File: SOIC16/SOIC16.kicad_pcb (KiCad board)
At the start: 2 copper layers, 20.3 x 12.7 mm, 7 parts, among them J1 Conn_02x08_Counter_Clockwise, J2 Conn_01x08, J3 Conn_01x08

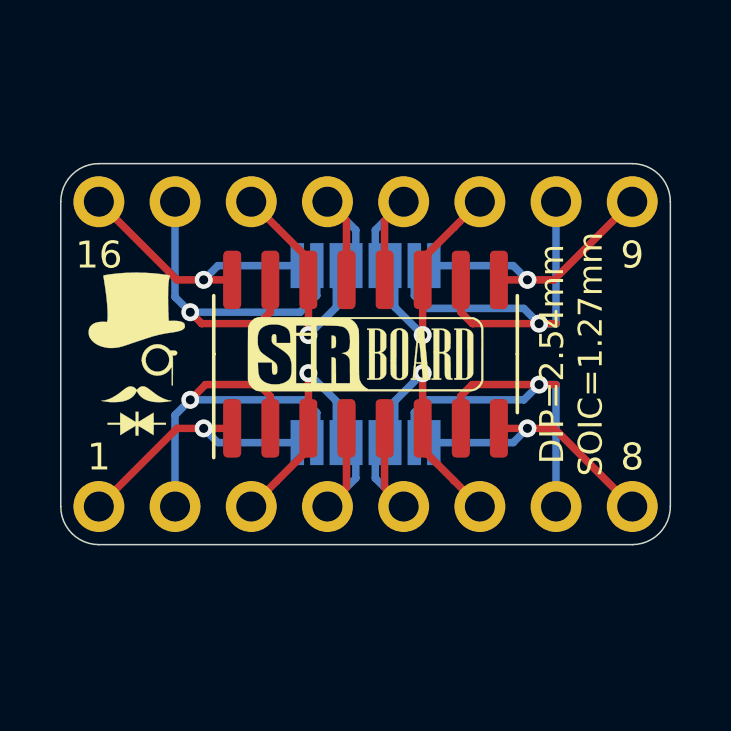
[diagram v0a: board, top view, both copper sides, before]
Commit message: convert SOIC16 to kicad 7
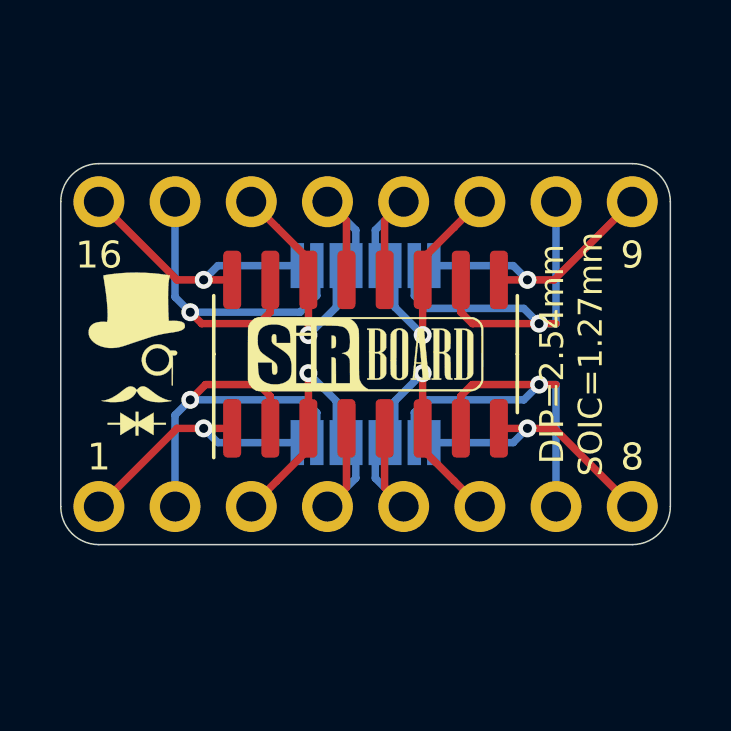
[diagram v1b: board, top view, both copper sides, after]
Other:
- net class Default removed

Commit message: add SOIC-Wide-16
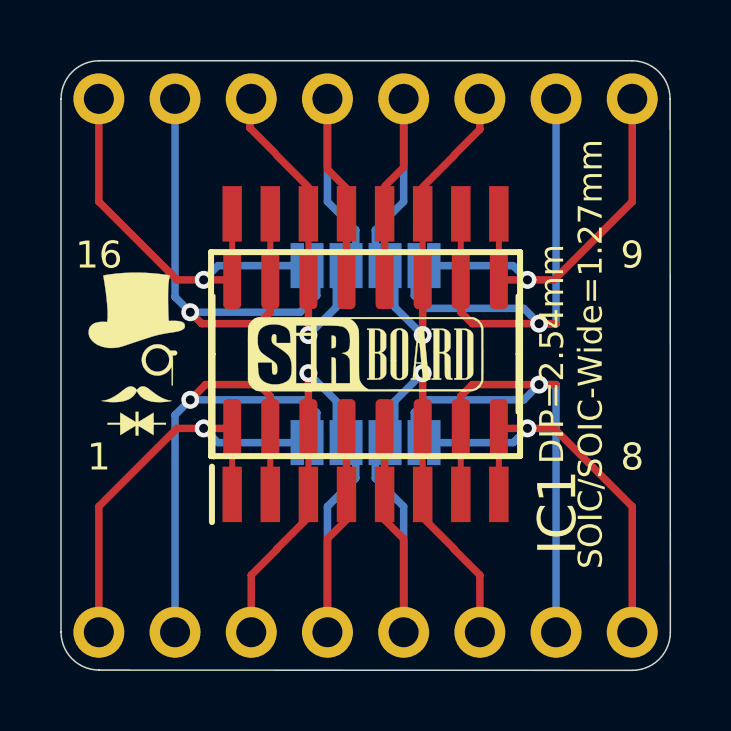
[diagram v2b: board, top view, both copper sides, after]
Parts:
- added IC1: SI8622ED-B-ISR 5kV, Kernelport:SOIC127P1030X265-16N, F.Cu at (66.4, 36.4)
- moved J3 4.19 mm to (57.5, 45.7)
- moved J2 3.43 mm to (57.5, 27.9)
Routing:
- net Net-(J1-Pad5): track 5.39 -> 12.7 mm
- net Net-(J1-Pad4): track 5.39 -> 12.7 mm
- net Net-(J1-Pad13): track 5.39 -> 11.2 mm
- net Net-(J1-Pad12): track 5.39 -> 11.1 mm
- net Net-(J1-Pad8): track 8.84 -> 13.0 mm
- net Net-(J1-Pad7): track 14.6 -> 18.8 mm
- net Net-(J1-Pad2): track 13.3 -> 17.5 mm
- net Net-(J1-Pad1): track 8.84 -> 13.0 mm
- net Net-(J1-Pad9): track 8.84 -> 12.3 mm
- net Net-(J1-Pad16): track 8.84 -> 12.3 mm
- net Net-(J1-Pad15): track 13.4 -> 16.8 mm
- net Net-(J1-Pad10): track 14.6 -> 18.0 mm
- net Net-(J1-Pad3): track 7.93 -> 9.84 mm
- net Net-(J1-Pad6): track 7.93 -> 9.84 mm
- net Net-(J1-Pad11): track 7.93 -> 8.95 mm
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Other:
- board size 20.3 x 12.7 mm -> 20.3 x 20.3 mm
- board text added: "DIP=2.54mm SOIC/SOIC-Wide=1.27mm"
- board text removed: "DIP=2.54mm SOIC=1.27mm"
